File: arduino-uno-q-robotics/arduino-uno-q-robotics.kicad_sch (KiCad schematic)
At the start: 19 parts, among them J1 Conn_02x30_Odd_Even, J2 Conn_02x30_Odd_Even, J3 Connector_FFC-FPC, J4 Connector_FFC-FPC, J5 Conn_02x13_Odd_Even, J6 Conn_02x04_Odd_Even, U1 LSM6DSO32, U2 TCA9803, U4 TCA9803

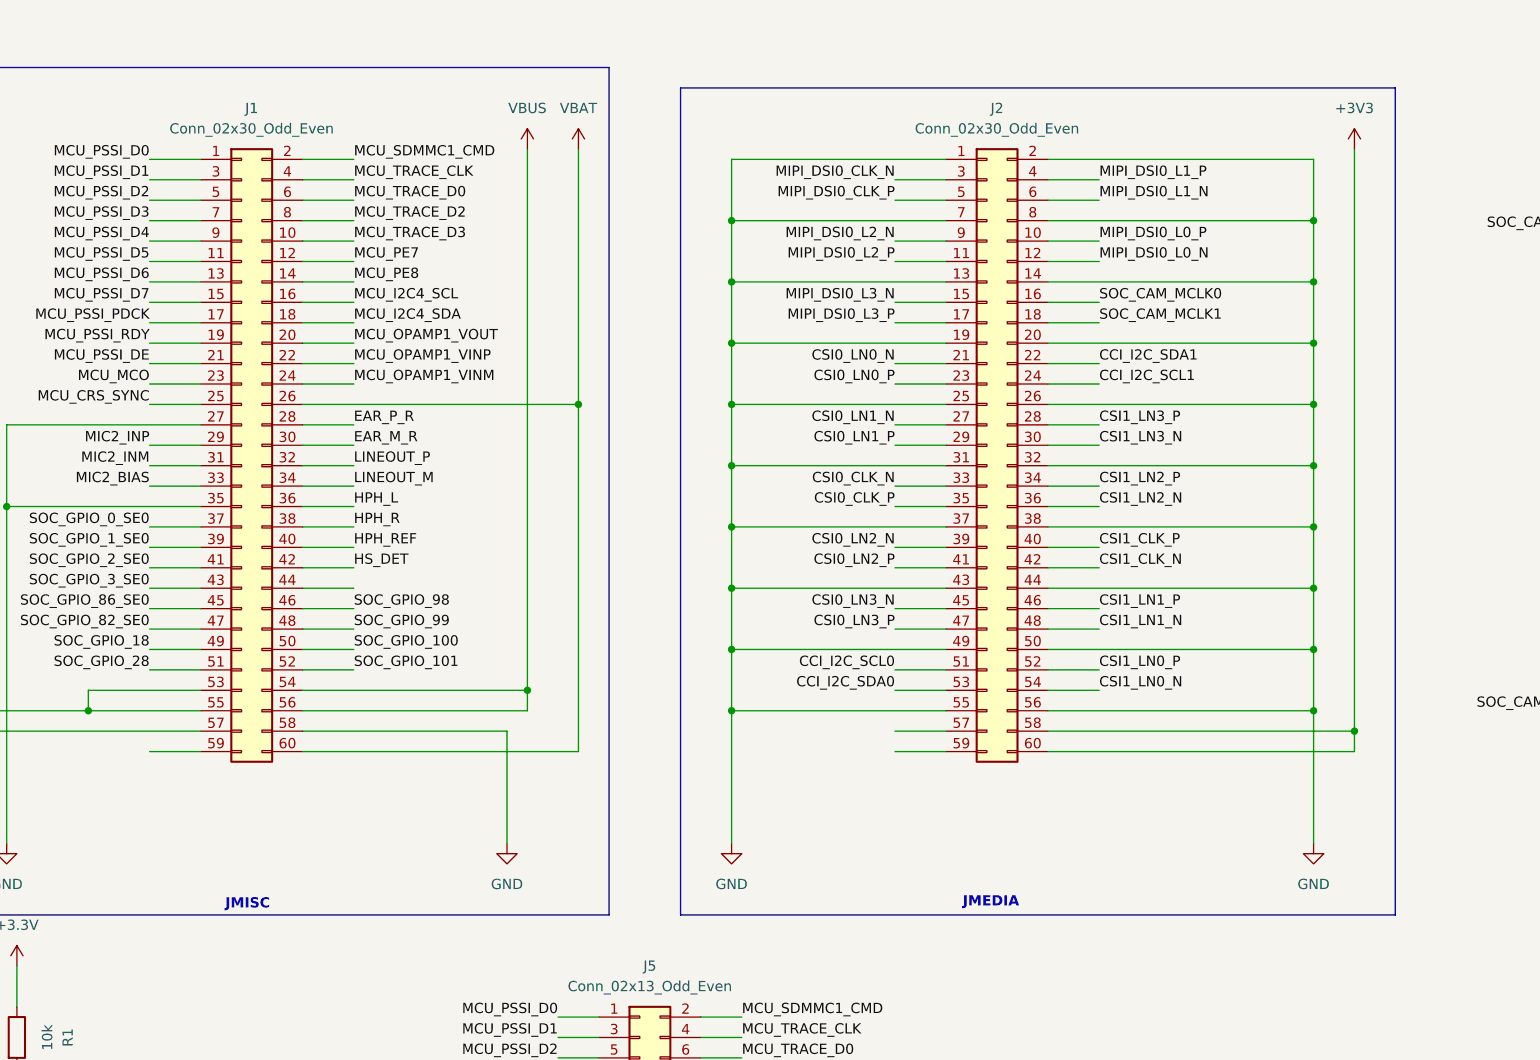
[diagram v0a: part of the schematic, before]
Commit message: Add missing pin functions to JMISC/MEDIA
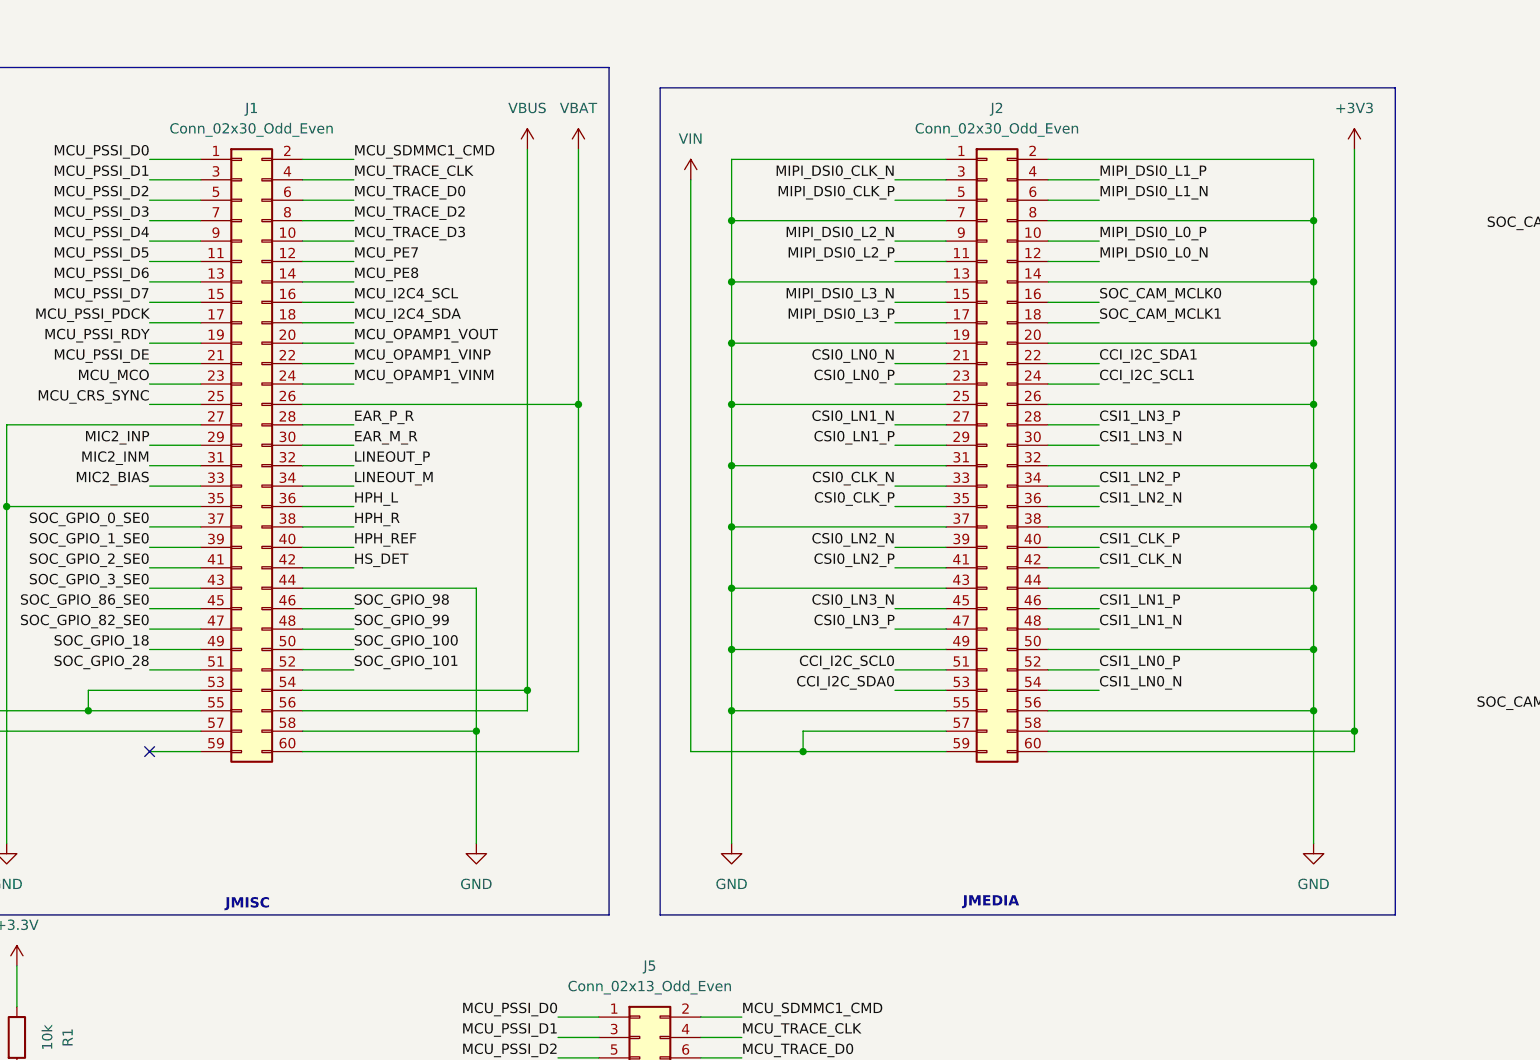
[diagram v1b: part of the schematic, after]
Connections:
- net GND: now also J1.44 (Pin_44)
- net VIN: now reaches J2.57 (Pin_57)
- net VIN: now also J2.59 (Pin_59)
- no-connect marks 7 -> 8
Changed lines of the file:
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@@
 	)
 	(rectangle
-		(start 119.38 22.86)
+		(start 116.84 22.86)
 		(end 208.28 125.73)
 		(stroke
@@
 	)
 	(junction
+		(at 93.98 102.87)
+		(diameter 0)
+		(color 0 0 0 0)
+	)
+	(junction
 		(at 125.73 92.71)
 		(diameter 0)
@@
 	)
 	(junction
-		(at 125.73 54.61)
+		(at 100.33 97.79)
 		(diameter 0)
 		(color 0 0 0 0)
 	)
 	(junction
-		(at 100.33 97.79)
+		(at 125.73 54.61)
 		(diameter 0)
 		(color 0 0 0 0)
@@
 	)
 	(junction
+		(at 134.62 105.41)
+		(diameter 0)
+		(color 0 0 0 0)
+	)
+	(junction
 		(at 106.68 62.23)
 		(diameter 0)
@@
 	)
 	(no_connect
+		(at 53.34 105.41)
+	)
+	(no_connect
 		(at 260.35 105.41)
 	)
@@
 	(wire
 		(pts
+			(xy 134.62 102.87) (xy 152.4 102.87)
+		)
+		(stroke
+			(width 0)
+			(type default)
+		)
+	)
+	(wire
+		(pts
 			(xy 104.14 190.5) (xy 107.95 190.5)
 		)
@@
 	(wire
 		(pts
+			(xy 120.65 105.41) (xy 134.62 105.41)
+		)
+		(stroke
+			(width 0)
+			(type default)
+		)
+	)
+	(wire
+		(pts
 			(xy 240.03 97.79) (xy 233.68 97.79)
 		)
@@
 	(wire
 		(pts
+			(xy 120.65 105.41) (xy 120.65 34.29)
+		)
+		(stroke
+			(width 0)
+			(type default)
+		)
+	)
+	(wire
+		(pts
 			(xy 377.19 101.6) (xy 381 101.6)
 		)
@@
 	(wire
 		(pts
-			(xy 146.05 105.41) (xy 152.4 105.41)
-		)
-		(stroke
-			(width 0)
-			(type default)
-		)
-	)
-	(wire
-		(pts
 			(xy 104.14 168.91) (xy 109.22 168.91)
 		)
@@
 	(wire
 		(pts
+			(xy 134.62 102.87) (xy 134.62 105.41)
+		)
+		(stroke
+			(width 0)
+			(type default)
+		)
+	)
+	(wire
+		(pts
 			(xy 36.83 132.08) (xy 36.83 137.16)
 		)
@@
 	(wire
 		(pts
-			(xy 72.39 102.87) (xy 97.79 102.87)
+			(xy 72.39 102.87) (xy 93.98 102.87)
 		)
 		(stroke
@@
 	(wire
 		(pts
+			(xy 93.98 85.09) (xy 93.98 102.87)
+		)
+		(stroke
+			(width 0)
+			(type default)
+		)
+	)
+	(wire
+		(pts
 			(xy 265.43 97.79) (xy 265.43 92.71)
 		)
@@
 	(wire
 		(pts
-			(xy 78.74 85.09) (xy 72.39 85.09)
+			(xy 72.39 85.09) (xy 93.98 85.09)
 		)
 		(stroke
@@
 	(wire
 		(pts
+			(xy 134.62 105.41) (xy 152.4 105.41)
+		)
+		(stroke
+			(width 0)
+			(type default)
+		)
+	)
+	(wire
+		(pts
 			(xy 165.1 69.85) (xy 198.12 69.85)
 		)
@@
 	(wire
 		(pts
-			(xy 146.05 102.87) (xy 152.4 102.87)
-		)
-		(stroke
-			(width 0)
-			(type default)
-		)
-	)
-	(wire
-		(pts
 			(xy 78.74 41.91) (xy 72.39 41.91)
 		)
@@
 	(wire
 		(pts
-			(xy 97.79 102.87) (xy 97.79 116.84)
+			(xy 93.98 102.87) (xy 93.98 116.84)
 		)
 		(stroke
@@
 	)
 	(symbol
+		(lib_id "power:VCC")
+		(at 120.65 34.29 0)
+		(unit 1)
+		(exclude_from_sim no)
+		(in_bom yes)
+		(on_board yes)
+		(dnp no)
+		(fields_autoplaced yes)
+		(property "Reference" "#PWR043"
+			(at 120.65 38.1 0)
+			(effects
+				(font
+					(size 1.27 1.27)
+				)
+				(hide yes)
+			)
+		)
+		(property "Value" "VIN"
+			(at 120.65 29.21 0)
+			(effects
+				(font
+					(size 1.27 1.27)
+				)
+			)
+		)
+		(property "Footprint" ""
+			(at 120.65 34.29 0)
+			(effects
+				(font
+					(size 1.27 1.27)
+				)
+				(hide yes)
+			)
+		)
+		(property "Datasheet" ""
+			(at 120.65 34.29 0)
+			(effects
+				(font
+					(size 1.27 1.27)
+				)
+				(hide yes)
+			)
+		)
+		(property "Description" "Power symbol creates a global label with name \"VIN\""
+			(at 120.65 34.29 0)
+			(effects
+				(font
+					(size 1.27 1.27)
+				)
+				(hide yes)
+			)
+		)
+		(pin "1"
+		)
+		(instances
+			(project ""
+				(path "/c2014409-d0b2-4c09-9f2e-87992017a082"
+					(reference "#PWR043")
+					(unit 1)
+				)
+			)
+		)
+	)
+	(symbol
 		(lib_id "power:+3.3V")
 		(at 29.21 167.64 0)
@@
 	(symbol
 		(lib_id "power:GND")
-		(at 97.79 116.84 0)
+		(at 93.98 116.84 0)
 		(unit 1)
 		(exclude_from_sim no)
@@
 		(fields_autoplaced yes)
 		(property "Reference" "#PWR06"
-			(at 97.79 123.19 0)
+			(at 93.98 123.19 0)
 			(effects
 				(font
@@
 		)
 		(property "Value" "GND"
-			(at 97.79 121.92 0)
+			(at 93.98 121.92 0)
 			(effects
 				(font
@@
 		)
 		(property "Footprint" ""
-			(at 97.79 116.84 0)
+			(at 93.98 116.84 0)
 			(effects
 				(font
@@
 		)
 		(property "Datasheet" ""
-			(at 97.79 116.84 0)
+			(at 93.98 116.84 0)
 			(effects
 				(font
@@
 		)
 		(property "Description" "Power symbol creates a global label with name \"GND\" , ground"
-			(at 97.79 116.84 0)
+			(at 93.98 116.84 0)
 			(effects
 				(font

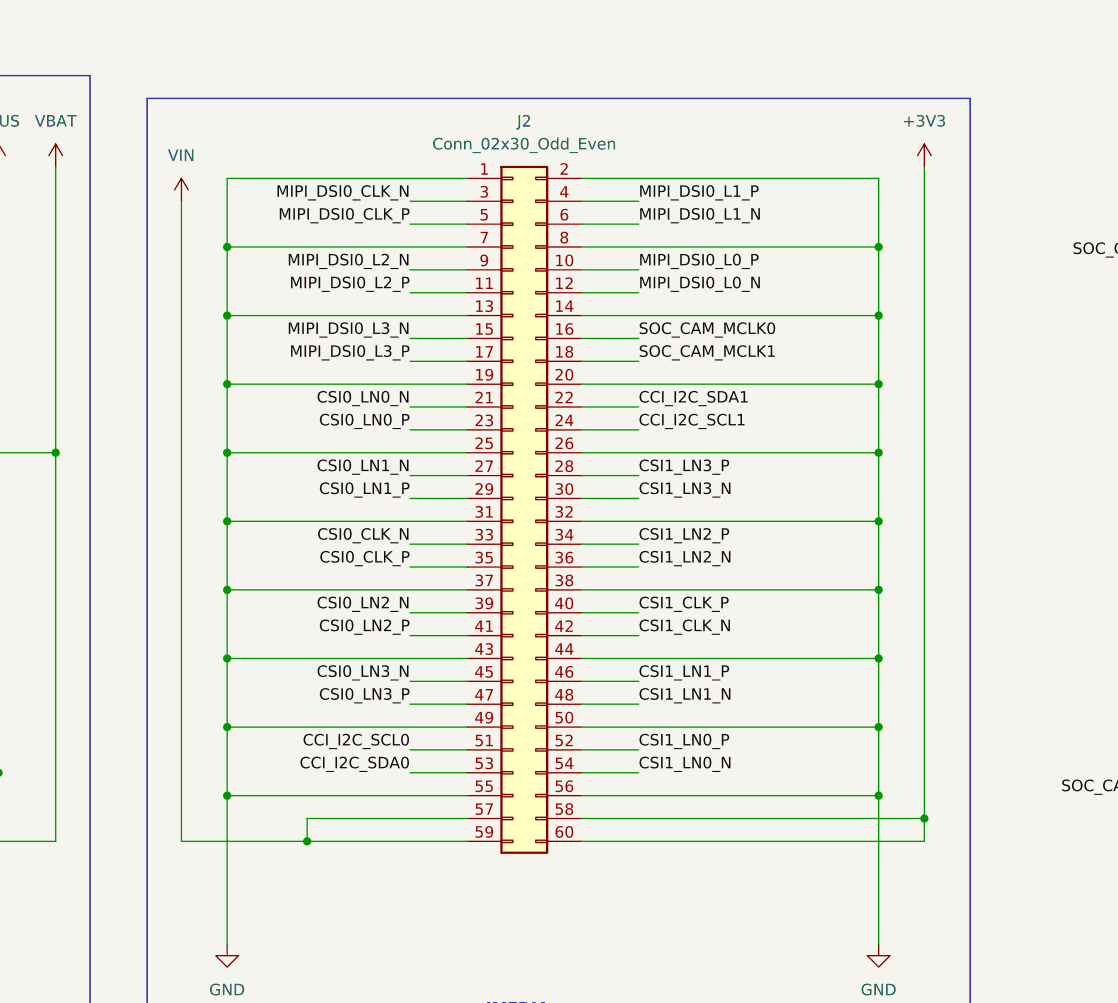
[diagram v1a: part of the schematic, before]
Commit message: Adjust power symbols
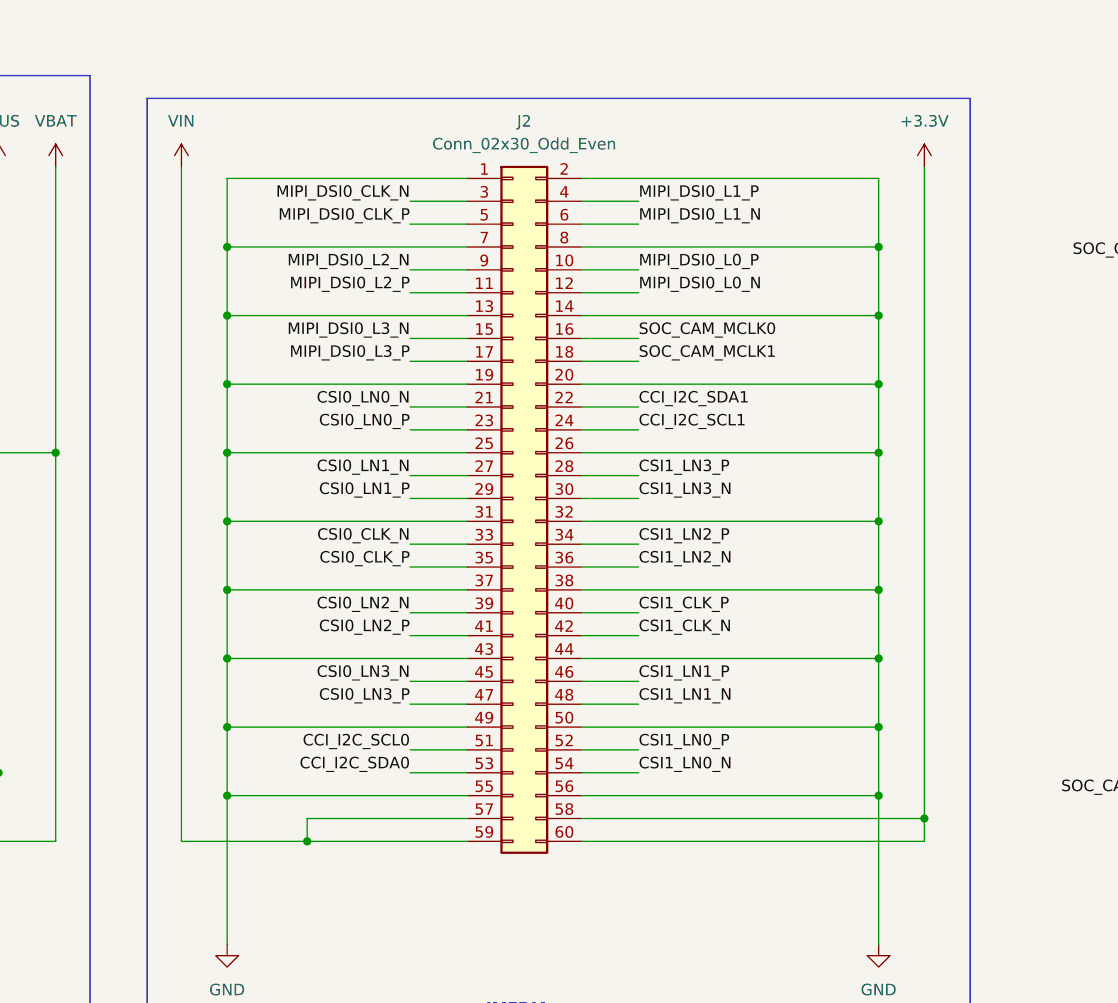
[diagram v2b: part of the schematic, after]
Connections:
- net +3V3 is gone; now on net +3.3V: J2.58 (Pin_58), J2.60 (Pin_60)
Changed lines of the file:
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@@
 	(wire
 		(pts
-			(xy 120.65 105.41) (xy 120.65 34.29)
+			(xy 120.65 105.41) (xy 120.65 30.48)
 		)
 		(stroke
@@
 	)
 	(symbol
-		(lib_id "power:+3V3")
-		(at 203.2 30.48 0)
-		(unit 1)
-		(exclude_from_sim no)
-		(in_bom yes)
-		(on_board yes)
-		(dnp no)
-		(fields_autoplaced yes)
-		(property "Reference" "#PWR09"
-			(at 203.2 34.29 0)
-			(effects
-				(font
-					(size 1.27 1.27)
-				)
-				(hide yes)
-			)
-		)
-		(property "Value" "+3V3"
-			(at 203.2 25.4 0)
-			(effects
-				(font
-					(size 1.27 1.27)
-				)
-			)
-		)
-		(property "Footprint" ""
-			(at 203.2 30.48 0)
-			(effects
-				(font
-					(size 1.27 1.27)
-				)
-				(hide yes)
-			)
-		)
-		(property "Datasheet" ""
-			(at 203.2 30.48 0)
-			(effects
-				(font
-					(size 1.27 1.27)
-				)
-				(hide yes)
-			)
-		)
-		(property "Description" "Power symbol creates a global label with name \"+3V3\""
-			(at 203.2 30.48 0)
-			(effects
-				(font
-					(size 1.27 1.27)
-				)
-				(hide yes)
-			)
-		)
-		(pin "1"
-		)
-		(instances
-			(project ""
-				(path "/c2014409-d0b2-4c09-9f2e-87992017a082"
-					(reference "#PWR09")
-					(unit 1)
-				)
-			)
-		)
-	)
-	(symbol
 		(lib_id "power:+3.3V")
 		(at 344.17 118.11 0)
@@
 	)
 	(symbol
+		(lib_id "power:+3.3V")
+		(at 203.2 30.48 0)
+		(unit 1)
+		(exclude_from_sim no)
+		(in_bom yes)
+		(on_board yes)
+		(dnp no)
+		(fields_autoplaced yes)
+		(property "Reference" "#PWR09"
+			(at 203.2 34.29 0)
+			(effects
+				(font
+					(size 1.27 1.27)
+				)
+				(hide yes)
+			)
+		)
+		(property "Value" "+3.3V"
+			(at 203.2 25.4 0)
+			(effects
+				(font
+					(size 1.27 1.27)
+				)
+			)
+		)
+		(property "Footprint" ""
+			(at 203.2 30.48 0)
+			(effects
+				(font
+					(size 1.27 1.27)
+				)
+				(hide yes)
+			)
+		)
+		(property "Datasheet" ""
+			(at 203.2 30.48 0)
+			(effects
+				(font
+					(size 1.27 1.27)
+				)
+				(hide yes)
+			)
+		)
+		(property "Description" "Power symbol creates a global label with name \"+3.3V\""
+			(at 203.2 30.48 0)
+			(effects
+				(font
+					(size 1.27 1.27)
+				)
+				(hide yes)
+			)
+		)
+		(pin "1"
+		)
+		(instances
+			(project "arduino-uno-q-robotics"
+				(path "/c2014409-d0b2-4c09-9f2e-87992017a082"
+					(reference "#PWR09")
+					(unit 1)
+				)
+			)
+		)
+	)
+	(symbol
 		(lib_id "power:GND")
 		(at 363.22 76.2 0)
@@
 	(symbol
 		(lib_id "power:VCC")
-		(at 120.65 34.29 0)
+		(at 120.65 30.48 0)
 		(unit 1)
 		(exclude_from_sim no)
@@
 		(fields_autoplaced yes)
 		(property "Reference" "#PWR043"
-			(at 120.65 38.1 0)
+			(at 120.65 34.29 0)
 			(effects
 				(font
@@
 		)
 		(property "Value" "VIN"
-			(at 120.65 29.21 0)
+			(at 120.65 25.4 0)
 			(effects
 				(font
@@
 		)
 		(property "Footprint" ""
-			(at 120.65 34.29 0)
+			(at 120.65 30.48 0)
 			(effects
 				(font
@@
 		)
 		(property "Datasheet" ""
-			(at 120.65 34.29 0)
+			(at 120.65 30.48 0)
 			(effects
 				(font
@@
 		)
 		(property "Description" "Power symbol creates a global label with name \"VIN\""
-			(at 120.65 34.29 0)
+			(at 120.65 30.48 0)
 			(effects
 				(font
